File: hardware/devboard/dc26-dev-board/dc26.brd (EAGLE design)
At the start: 126 x 70 mm, 112 parts, among them CN1 JST, IC3 LDL112D33R, J1 DC26 Shitty AddOn, J2 DC26 Shitty AddOn, P1 SSSS811101, Y1 ABL-8.000MHZ-B2

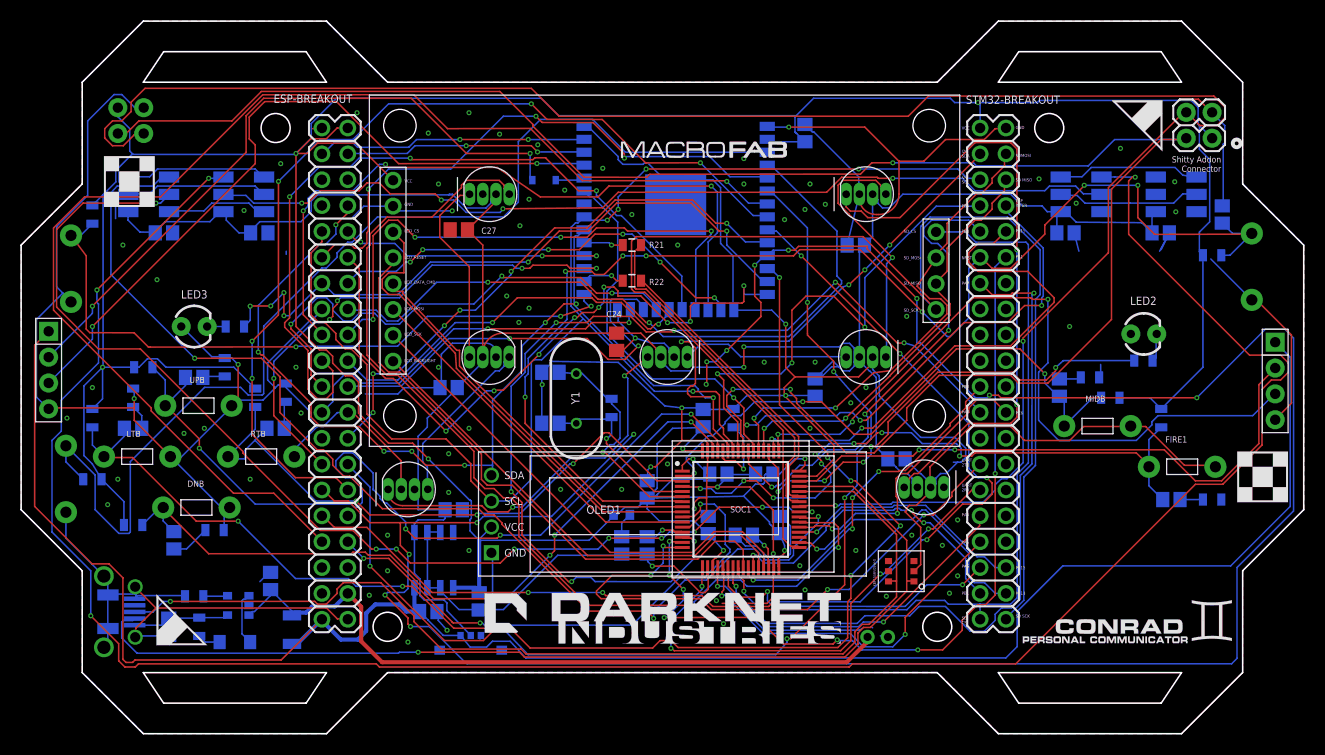
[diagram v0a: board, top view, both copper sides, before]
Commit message: removed vin from esp and stm32 programer headers you will need to have battery connected to program
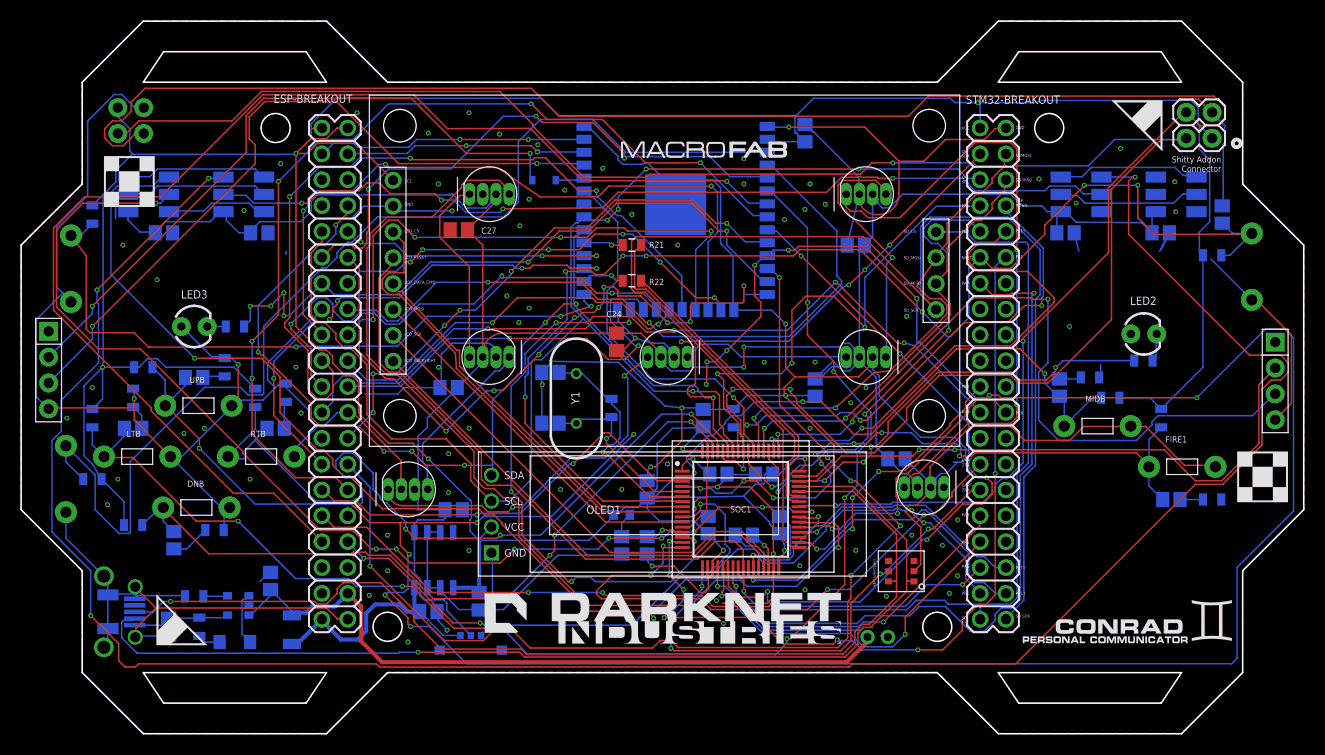
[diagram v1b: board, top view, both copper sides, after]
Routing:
- net VIN: track 191.5 -> 24.8 mm
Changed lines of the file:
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@@
 <?xml version="1.0" encoding="utf-8"?>
 <!DOCTYPE eagle SYSTEM "eagle.dtd">
-<eagle version="8.7.1">
+<eagle version="9.0.1">
 <drawing>
 <settings>
@@
 <wire x1="41.9714" y1="11.1553125" x2="43.4767125" y2="9.65" width="0.1524" layer="16"/>
 <wire x1="43.4767125" y1="9.65" x2="45.17" y2="9.65" width="0.1524" layer="16"/>
-<wire x1="125.2" y1="38.46" x2="126.673815625" y2="36.986184375" width="0.1524" layer="16"/>
-<wire x1="126.673815625" y1="36.986184375" x2="126.673815625" y2="22.326184375" width="0.1524" layer="16"/>
-<wire x1="126.673815625" y1="22.326184375" x2="120.8316" y2="16.48396875" width="0.1524" layer="16"/>
-<wire x1="120.8316" y1="16.48396875" x2="104.33396875" y2="16.48396875" width="0.1524" layer="16"/>
-<wire x1="104.33396875" y1="16.48396875" x2="99.85" y2="12" width="0.1524" layer="16"/>
-<wire x1="99.85" y1="12" x2="99.85" y2="8.55" width="0.1524" layer="16"/>
-<wire x1="99.85" y1="8.55" x2="98.740625" y2="7.440625" width="0.1524" layer="16"/>
-<wire x1="51.5776625" y1="7.440625" x2="50.0396875" y2="9.0786" width="0.1524" layer="16"/>
-<wire x1="98.740625" y1="7.440625" x2="51.5776625" y2="7.440625" width="0.1524" layer="16"/>
-<wire x1="46.11085625" y1="8.50914375" x2="45.17" y2="9.65" width="0.1524" layer="16"/>
-<wire x1="50.0396875" y1="9.0786" x2="48.3003125" y2="9.0786" width="0.1524" layer="16"/>
-<wire x1="47.73085625" y1="8.50914375" x2="46.11085625" y2="8.50914375" width="0.1524" layer="16"/>
-<wire x1="48.3003125" y1="9.0786" x2="47.73085625" y2="8.50914375" width="0.1524" layer="16"/>
-<wire x1="4.7" y1="39.53" x2="3.326184375" y2="38.156184375" width="0.1524" layer="1"/>
-<wire x1="3.326184375" y1="38.156184375" x2="3.326184375" y2="22.326184375" width="0.1524" layer="1"/>
-<wire x1="3.326184375" y1="22.326184375" x2="8.96876875" y2="16.6836" width="0.1524" layer="1"/>
-<wire x1="8.96876875" y1="16.6836" x2="10.62855" y2="16.6836" width="0.1524" layer="1"/>
-<wire x1="10.62855" y1="16.6836" x2="12" y2="15.31215" width="0.1524" layer="1"/>
-<wire x1="12" y1="15.31215" x2="12" y2="7.3" width="0.1524" layer="1"/>
-<wire x1="12" y1="7.3" x2="12.3" y2="7" width="0.1524" layer="1"/>
-<wire x1="12.3" y1="7" x2="12.94763125" y2="7" width="0.1524" layer="1"/>
-<wire x1="27.550625" y1="7.240625" x2="31.55" y2="11.24" width="0.1524" layer="1"/>
-<wire x1="12.94763125" y1="7" x2="13.18825625" y2="7.240625" width="0.1524" layer="1"/>
-<wire x1="13.18825625" y1="7.240625" x2="27.550625" y2="7.240625" width="0.1524" layer="1"/>
+<wire x1="45.17" y1="9.65" x2="125.2" y2="38.46" width="0" layer="19" extent="16-16"/>
+<wire x1="4.7" y1="39.53" x2="28.61" y2="8.82" width="0" layer="19" extent="16-16"/>
 </signal>
 <signal name="ESP-RX" airwireshidden="yes">
@@
 </signal>
 </signals>
+<errors>
+</errors>
 </board>
 </drawing>

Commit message: adding real data sheet for switch
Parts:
- P1: value SSSS811101 -> SPDT_SSAJ120100
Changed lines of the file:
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@@
 <attribute name="NAME" x="59.23" y="21.6" size="0.8128" layer="25" font="vector" align="bottom-center"/>
 </element>
-<element name="P1" library="dc-26" package="SPDT_SSAJ120100" value="SSSS811101" x="46.17" y="8.2" smashed="yes" rot="MR0"/>
+<element name="P1" library="dc-26" package="SPDT_SSAJ120100" value="SPDT_SSAJ120100" x="46.17" y="8.2" smashed="yes" rot="MR0"/>
 <element name="R1" library="dc-26" package="0805" value="10K" x="9" y="51" smashed="yes" rot="MR90">
 <attribute name="NAME" x="9.8255" y="50.238" size="0.6096" layer="26" font="vector" rot="MR90"/>
